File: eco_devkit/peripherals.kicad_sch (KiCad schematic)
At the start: 0 parts

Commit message: feat: implement GPIO peripherals (buttons, LEDs, buzzer, MOSFET)
- Infrared not included
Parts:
- added BZ1: WT-1205, Buzzer_Beeper:Buzzer_12mm_P5.0mm_Vertical, symbol Device:Buzzer
- added D1: LED_Red, LED_SMD:LED_1206_3216Metric, symbol Device:LED
- added D2: LED_Green, LED_SMD:LED_1206_3216Metric, symbol Device:LED
- added D3: LED_Blue, LED_SMD:LED_1206_3216Metric, symbol Device:LED
- added D4: LED_Yellow, LED_SMD:LED_1206_3216Metric, symbol Device:LED
- added D5: WS2812B, LED_SMD:LED_WS2812B_PLCC4_5.0x5.0mm_P3.2mm, symbol LED:WS2812B
- added J_BUTTONS, J_LEDS: Conn_02x04_Counter_Clockwise, symbol Connector_Generic:Conn_02x04_Counter_Clockwise
- added J_MOSFET: Conn_02x02_Counter_Clockwise, symbol Connector_Generic:Conn_02x02_Counter_Clockwise
- added Q1: 2N2219, Package_TO_SOT_THT:TO-39-3, symbol Transistor_BJT:2N2219
- added Q2: Q_NMOS_GDS, symbol Transistor_FET:Q_NMOS_GDS
- added R1: 150Ω, symbol Device:R
- added R2: 120Ω, symbol Device:R
- added R3: 33Ω, symbol Device:R
- added R4: 130Ω, symbol Device:R
- added R5, R7: 330ohm, symbol Device:R
- added R6: 100ohm, symbol Device:R
- added SW1, SW2, SW3, SW4: TL2202, Button_Switch_SMD:SW_SPST_TL2202, symbol Switch:SW_Push
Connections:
- new net: D3.2 (A), R3.1
- new net: D2.2 (A), R2.1
- new net: D4.2 (A), R4.1
- new net: BZ1.2 (-), Q1.3 (C)
- new net: Q2.1 (G), R6.2
- new net: D1.2 (A), R1.1
- new net: Q1.2 (B), R5.2
- new net: D5.4 (DIN), R7.2
- new net +5V: BZ1.1 (+), D5.1 (VDD)
- new net GND: D1.1 (K), D2.1 (K), D3.1 (K), D4.1 (K), D5.3 (VSS), Q1.1 (E), Q2.3 (S), SW1.1, SW2.1, SW3.1, SW4.1
- new net GPIO_MOSFET_CONECTOR: Q2.2 (D)
- no-connect marks 0 -> 1

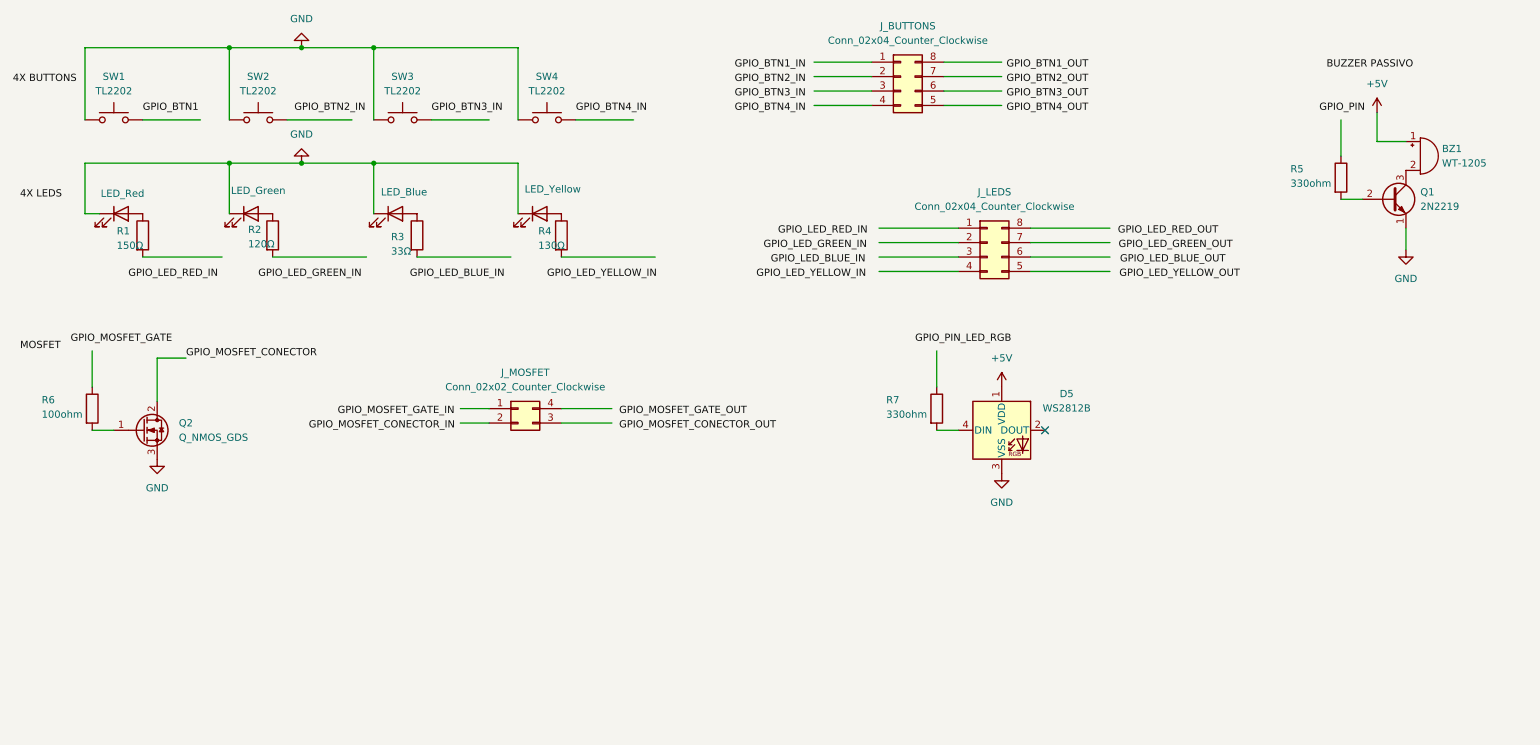
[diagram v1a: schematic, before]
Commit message: chore: ajustes nos periféricos GPIO e mapeamento do conector SWD
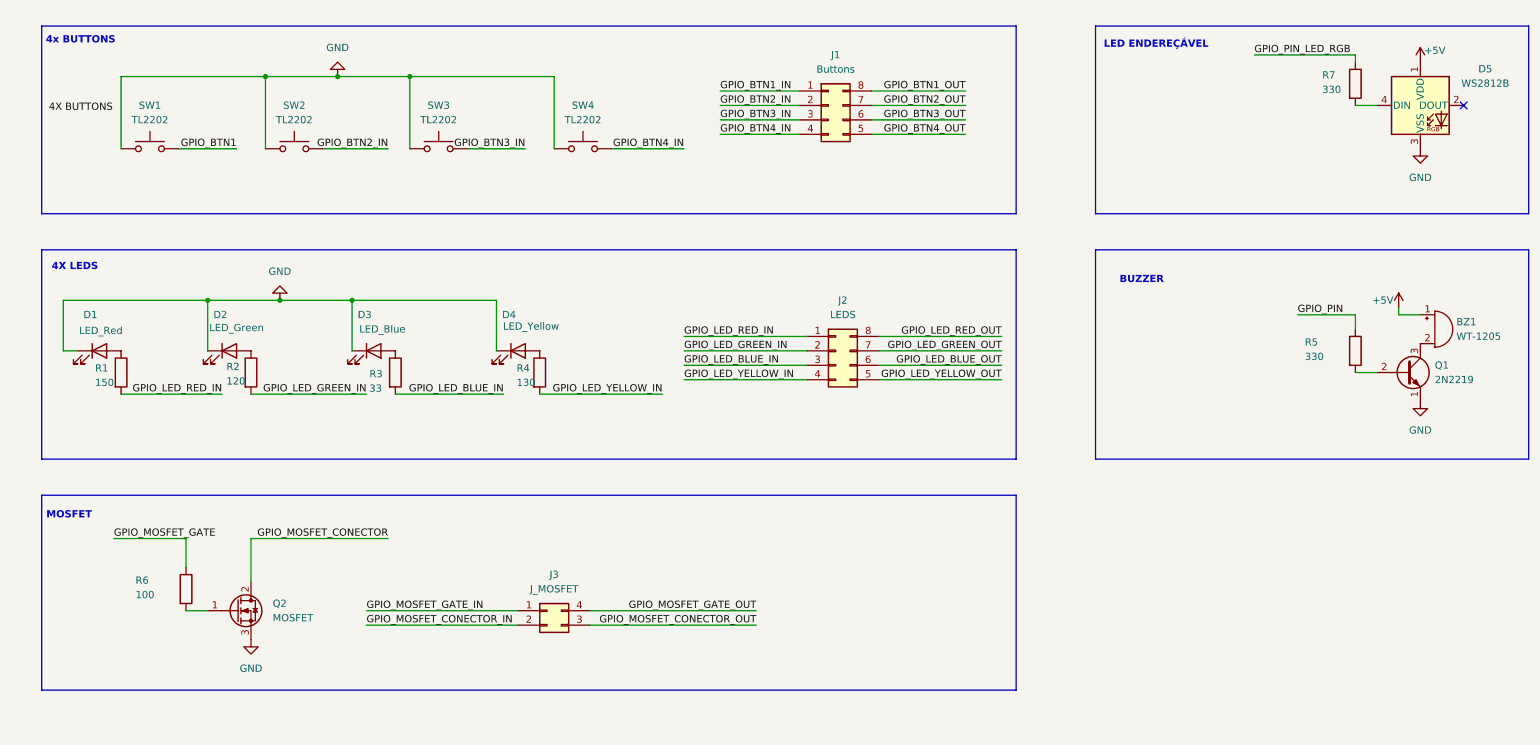
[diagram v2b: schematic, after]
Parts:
- J1: renamed from J_BUTTONS; value Conn_02x04_Counter_Clockwise -> Buttons
- J2: renamed from J_LEDS; value Conn_02x04_Counter_Clockwise -> LEDS
- J3: renamed from J_MOSFET; value Conn_02x02_Counter_Clockwise -> J_MOSFET
- Q2: value Q_NMOS_GDS -> MOSFET
- R1: value 150Ω -> 150
- R2: value 120Ω -> 120
- R3: value 33Ω -> 33
- R4: value 130Ω -> 130
- R5, R7: value 330ohm -> 330
- R6: value 100ohm -> 100
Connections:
- net GPIO_BTN1: now also SW1.2
- net GPIO_BTN1_IN: now also J1.1 (Pin_1)
- net GPIO_BTN1_OUT: now also J1.8 (Pin_8)
- net GPIO_BTN2_IN: now also J1.2 (Pin_2), SW2.2
- net GPIO_BTN2_OUT: now also J1.7 (Pin_7)
- net GPIO_BTN3_IN: now also J1.3 (Pin_3), SW3.2
- net GPIO_BTN3_OUT: now also J1.6 (Pin_6)
- net GPIO_BTN4_IN: now also J1.4 (Pin_4), SW4.2
- net GPIO_BTN4_OUT: now also J1.5 (Pin_5)
- net GPIO_LED_BLUE_IN: now also J2.3 (Pin_3), R3.2
- net GPIO_LED_BLUE_OUT: now also J2.6 (Pin_6)
- net GPIO_LED_GREEN_IN: now also J2.2 (Pin_2), R2.2
- net GPIO_LED_GREEN_OUT: now also J2.7 (Pin_7)
- net GPIO_LED_RED_IN: now also J2.1 (Pin_1), R1.2
- net GPIO_LED_RED_OUT: now also J2.8 (Pin_8)
- net GPIO_LED_YELLOW_IN: now also J2.4 (Pin_4), R4.2
- net GPIO_LED_YELLOW_OUT: now also J2.5 (Pin_5)
- net GPIO_MOSFET_CONECTOR_IN: now also J3.2 (Pin_2)
- net GPIO_MOSFET_CONECTOR_OUT: now also J3.3 (Pin_3)
- net GPIO_MOSFET_GATE: now also R6.1
- net GPIO_MOSFET_GATE_IN: now also J3.1 (Pin_1)
- net GPIO_MOSFET_GATE_OUT: now also J3.4 (Pin_4)
- net GPIO_PIN: now also R5.1
- net GPIO_PIN_LED_RGB: now also R7.1
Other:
- note added: "4X LEDS"
- note added: "4x BUTTONS"
- note added: "BUZZER"
- note added: "LED ENDEREÇÁVEL"
- note added: "MOSFET"
- moved on the sheet: BZ1, D5, J1, J2, J3, Q1, Q2, R1, R2, R3, R4, R5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

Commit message: Add bluetooth.
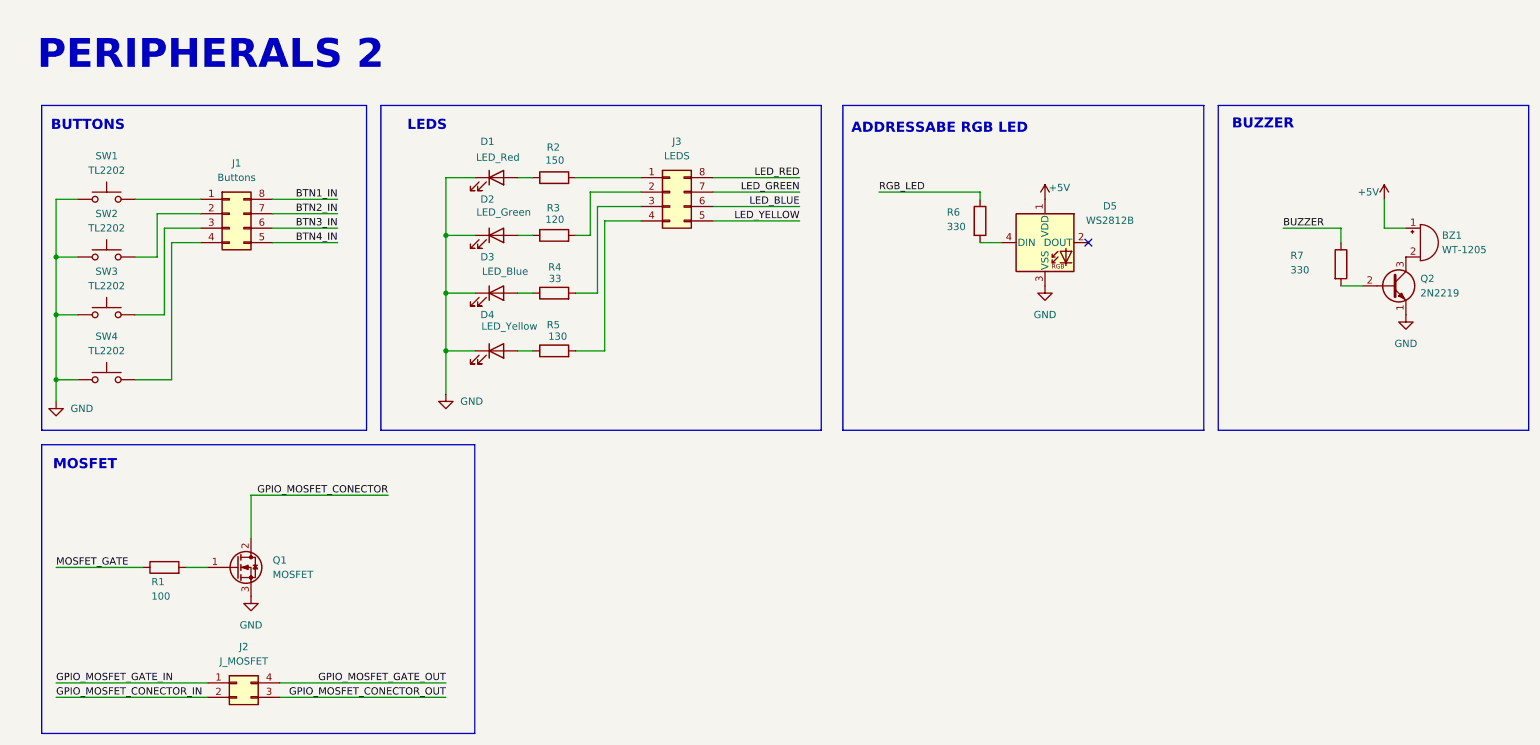
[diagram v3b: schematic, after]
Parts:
- J1: footprint (none) -> Connector_PinHeader_2.54mm:PinHeader_2x04_P2.54mm_Vertical
- J3: renamed from J2; footprint (none) -> Connector_PinHeader_2.54mm:PinHeader_2x04_P2.54mm_Vertical
- R1: renamed from R6; footprint (none) -> Resistor_SMD:R_0402_1005Metric
- R2: renamed from R1; footprint (none) -> Resistor_SMD:R_0402_1005Metric
- R3: renamed from R2; footprint (none) -> Resistor_SMD:R_0402_1005Metric
- R4: renamed from R3; footprint (none) -> Resistor_SMD:R_0402_1005Metric
- R5: renamed from R4; footprint (none) -> Resistor_SMD:R_0402_1005Metric
- R6: renamed from R7; footprint (none) -> Resistor_SMD:R_0402_1005Metric
- R7: renamed from R5; footprint (none) -> Resistor_SMD:R_0402_1005Metric
- renumbered J3 to J2, Q2 to Q1, Q1 to Q2
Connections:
- net GPIO_BTN1_IN is gone; now on an unnamed net: J1.1 (Pin_1)
- net GPIO_BTN1: no longer names the net of SW1.2
- net GPIO_BTN1_OUT renamed BTN1_IN
- net GPIO_BTN2_IN: no longer names the net of J1.2 (Pin_2), SW2.2
- net GPIO_BTN2_OUT renamed BTN2_IN
- net GPIO_BTN3_IN: no longer names the net of J1.3 (Pin_3), SW3.2
- net GPIO_BTN3_OUT renamed BTN3_IN
- net GPIO_BTN4_IN: no longer names the net of J1.4 (Pin_4), SW4.2
- net GPIO_BTN4_OUT renamed BTN4_IN
- net GPIO_LED_BLUE_IN: no longer names the net of J3.3 (Pin_3), R4.2
- net GPIO_LED_BLUE_OUT renamed LED_BLUE
- net GPIO_LED_GREEN_IN: no longer names the net of J3.2 (Pin_2), R3.2
- net GPIO_LED_GREEN_OUT renamed LED_GREEN
- net GPIO_LED_RED_IN: no longer names the net of J3.1 (Pin_1), R2.2
- net GPIO_LED_RED_OUT renamed LED_RED
- net GPIO_LED_YELLOW_IN: no longer names the net of J3.4 (Pin_4), R5.2
- net GPIO_LED_YELLOW_OUT renamed LED_YELLOW
- net GPIO_MOSFET_GATE renamed MOSFET_GATE
- net GPIO_PIN renamed BUZZER
- net GPIO_PIN_LED_RGB renamed RGB_LED
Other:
- note added: "ADDRESSABE RGB LED"
- note added: "BUTTONS"
- note added: "LEDS"
- note added: "PERIPHERALS 2"
- note removed: "4X LEDS"
- note removed: "4x BUTTONS"
- note removed: "LED ENDEREÇÁVEL"
- moved on the sheet: BZ1, D1, D2, D3, D4, D5, J1, J2, J3, Q1, Q2, R1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

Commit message: First interation.
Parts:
- added U4: ~, symbol EcoDevkit:LTR-329ALS
- D5: MPN (none) -> 16347
- SW3: renamed from SW1; value TL2202 -> PTS636; footprint Button_Switch_SMD:SW_SPST_TL2202 -> Button_Switch_SMD:SW_Tactile_SPST_NO_Straight_CK_PTS636Sx25SMTRLFS; MPN (none) -> PTS636 SK43 SMTR LFS
- SW4: renamed from SW2; value TL2202 -> PTS636; footprint Button_Switch_SMD:SW_SPST_TL2202 -> Button_Switch_SMD:SW_Tactile_SPST_NO_Straight_CK_PTS636Sx25SMTRLFS; MPN (none) -> PTS636 SK43 SMTR LFS
- SW5: renamed from SW3; value TL2202 -> PTS636; footprint Button_Switch_SMD:SW_SPST_TL2202 -> Button_Switch_SMD:SW_Tactile_SPST_NO_Straight_CK_PTS636Sx25SMTRLFS; MPN (none) -> PTS636 SK43 SMTR LFS
- SW6: renamed from SW4; value TL2202 -> PTS636; footprint Button_Switch_SMD:SW_SPST_TL2202 -> Button_Switch_SMD:SW_Tactile_SPST_NO_Straight_CK_PTS636Sx25SMTRLFS; MPN (none) -> PTS636 SK43 SMTR LFS
- renumbered J1 to J3, J2 to J4, J3 to J5, R1 to R10, R2 to R11, R3 to R12, R4 to R13, R5 to R14, R6 to R15, R7 to R16
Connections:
- net +5V: no longer D5.1 (VDD)
- net GND: now also U4.2 (GND)
- new net +3V3: D5.1 (VDD), U4.1 (VDD)
- new net LIGHT_SENS_SCL: U4.4 (SCL)
- new net LIGHT_SENS_SDA: U4.3 (SDA)
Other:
- note added: "LIGHT SENSOR I2C"
